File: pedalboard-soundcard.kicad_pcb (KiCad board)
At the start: 2 copper layers, 65 x 56 mm, 81 parts, among them J1 RPi_GPIO, J2 Conn_02x03_Odd_Even, J3 Conn_02x03_Odd_Even, U1 AT24CS01-STUM, U2 NCP163, U3 NCP163, U4 PCM1863DBT, U5 NCP163, U6 PCM5242RHBR, X1 22.5792Mhz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

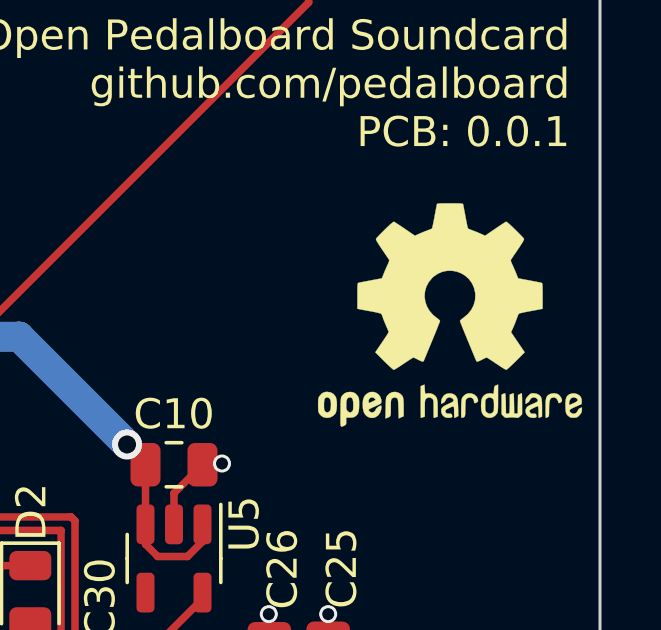
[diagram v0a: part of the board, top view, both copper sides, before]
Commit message: Smaller OSHW Logo
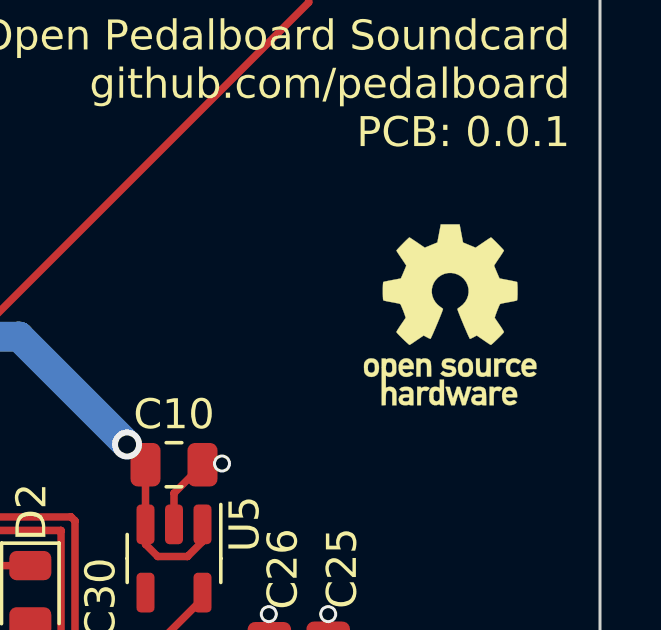
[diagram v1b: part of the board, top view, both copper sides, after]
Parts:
- SYM1: footprint Symbol:OSHW-Logo2_9.8x8mm_SilkScreen -> Symbol:OSHW-Logo_5.7x6mm_SilkScreen

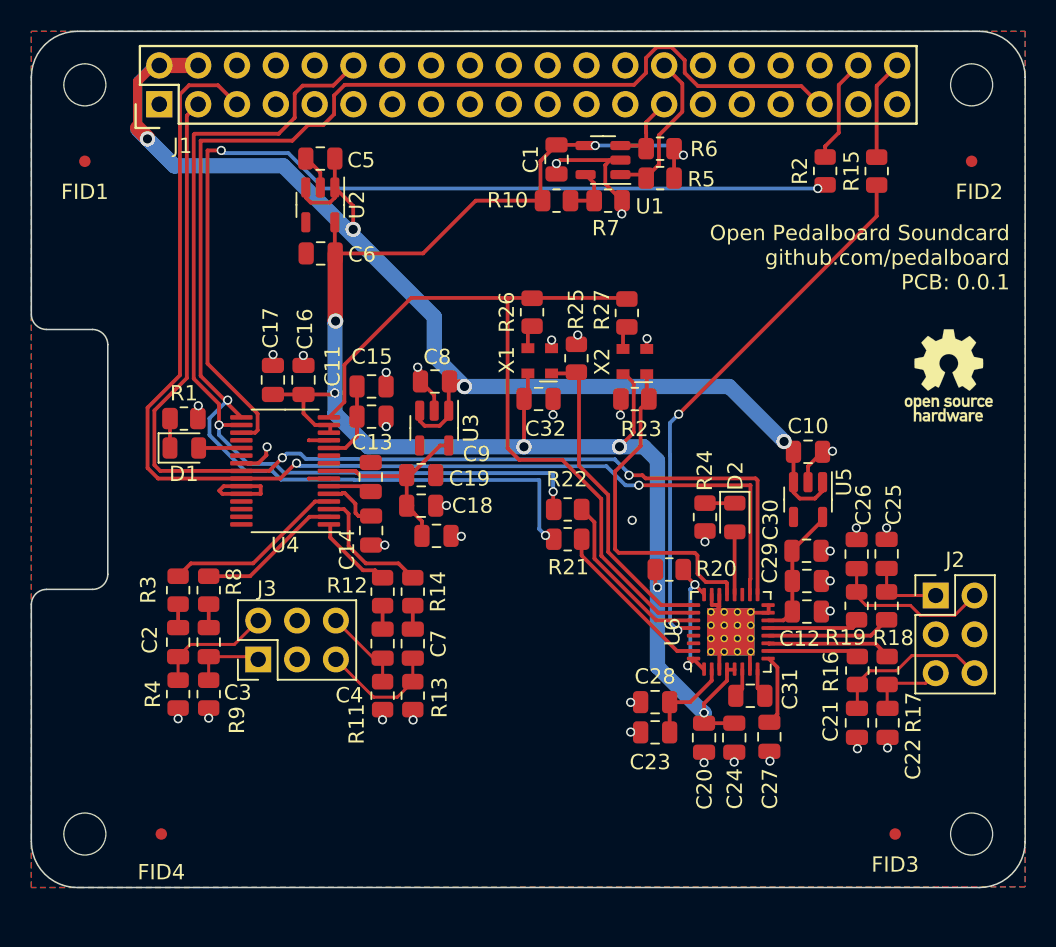
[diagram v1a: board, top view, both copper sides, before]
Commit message: Add texts for connectors
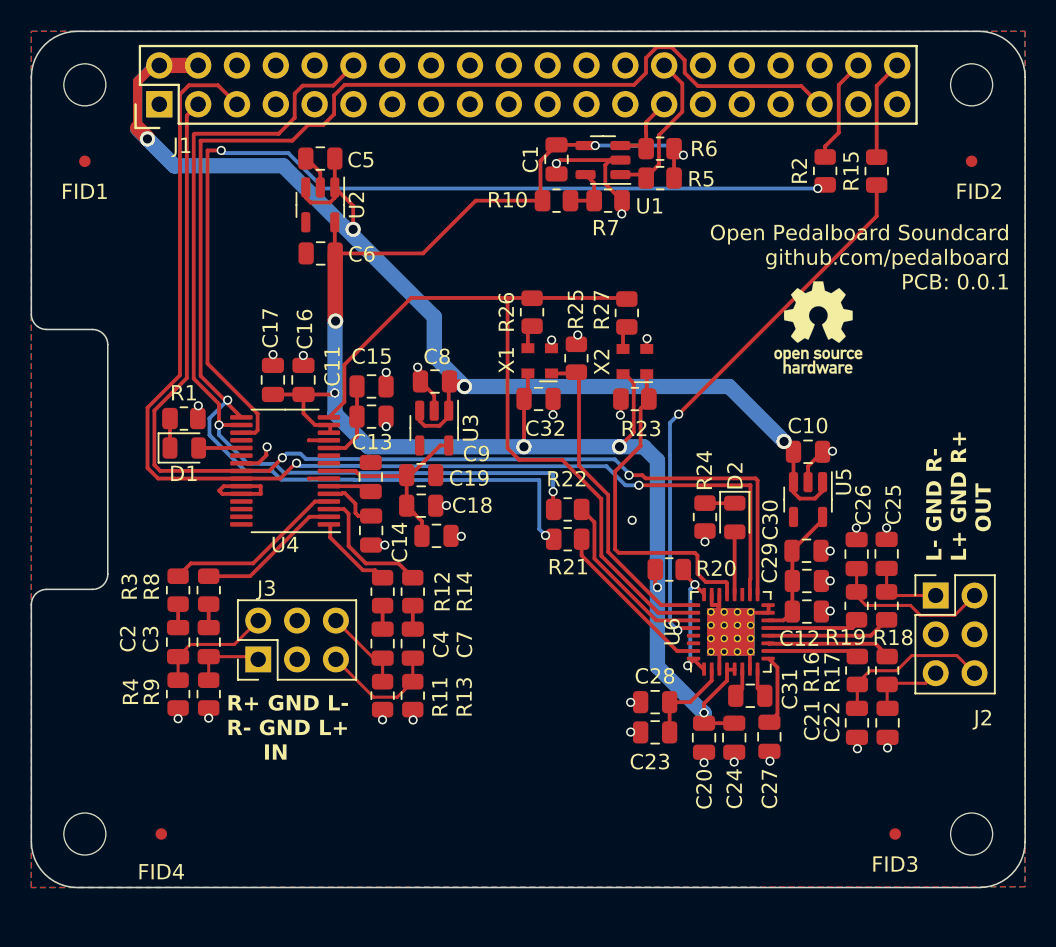
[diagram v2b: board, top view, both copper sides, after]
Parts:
- moved SYM1 9.09 mm to (100.0, 71.9)
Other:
- board text added: "L- GND R- L+ GND R+ OUT"
- board text added: "R+ GND L- R- GND L+ IN"
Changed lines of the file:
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@@
     (property "ki_keywords" "cap capacitor")
     (attr smd)
-    (fp_text reference "C21" (at -0.1 1.72 90) (layer "F.SilkS")
+    (fp_text reference "C21" (at -0.15 2.92 90) (layer "F.SilkS")
         (effects (font (size 1 1) (thickness 0.15)))
     )
@@
     (property "ki_keywords" "R res resistor")
     (attr smd)
-    (fp_text reference "R16" (at 0.075 1.725 90) (layer "F.SilkS")
+    (fp_text reference "R16" (at 0.105 2.975 90) (layer "F.SilkS")
         (effects (font (size 1 1) (thickness 0.15)))
     )
@@
     (property "ki_keywords" "cap capacitor")
     (attr smd)
-    (fp_text reference "C3" (at 3.3 -1.9 -180) (layer "F.SilkS")
+    (fp_text reference "C3" (at -0.2 3.77 -90) (layer "F.SilkS")
         (effects (font (size 1 1) (thickness 0.15)))
     )
@@
     (property "ki_keywords" "cap capacitor")
     (attr smd)
-    (fp_text reference "C14" (at -1.25 -1.575 90) (layer "F.SilkS")
+    (fp_text reference "C14" (at -0.77 1.885 90) (layer "F.SilkS")
         (effects (font (size 1 1) (thickness 0.15)))
     )
@@
     (property "ki_keywords" "cap capacitor")
     (attr smd)
-    (fp_text reference "C4" (at 3.375 2.175 -180) (layer "F.SilkS")
+    (fp_text reference "C4" (at 0.05 -3.845 -90) (layer "F.SilkS")
         (effects (font (size 1 1) (thickness 0.15)))
     )
@@
     (property "ki_keywords" "R res resistor")
     (attr smd)
-    (fp_text reference "R11" (at -1.85 -1.7 90) (layer "F.SilkS")
+    (fp_text reference "R11" (at -0.09 3.775 90) (layer "F.SilkS")
         (effects (font (size 1 1) (thickness 0.15)))
     )
@@
     (property "ki_keywords" "cap capacitor")
     (attr smd)
-    (fp_text reference "C7" (at 0 -1.68 90) (layer "F.SilkS")
+    (fp_text reference "C7" (at 0.05 -3.41 90) (layer "F.SilkS")
         (effects (font (size 1 1) (thickness 0.15)))
     )
@@
     (property "ki_keywords" "R res resistor")
     (attr smd)
-    (fp_text reference "R12" (at -0.4 2.325 -180) (layer "F.SilkS")
+    (fp_text reference "R12" (at 0 -3.925 -90) (layer "F.SilkS")
         (effects (font (size 1 1) (thickness 0.15)))
     )
@@
     (property "ki_keywords" "R res resistor")
     (attr smd)
-    (fp_text reference "R13" (at -0.125 1.75 90) (layer "F.SilkS")
+    (fp_text reference "R13" (at -0.09 3.39 90) (layer "F.SilkS")
         (effects (font (size 1 1) (thickness 0.15)))
     )
@@
   )
   (footprint "Symbol:OSHW-Logo_5.7x6mm_SilkScreen" (layer "F.Cu")
-    (at 108.5 75)
+    (at 99.97 71.87)
     (descr "Open Source Hardware Logo")
     (tags "Logo OSHW")
@@
     (property "ki_keywords" "connector")
     (attr through_hole)
-    (fp_text reference "J2" (at 1.27 -2.33) (layer "F.SilkS")
+    (fp_text reference "J2" (at 3.12 8.03) (layer "F.SilkS")
         (effects (font (size 1 1) (thickness 0.15)))
     )
@@
     (property "ki_keywords" "R res resistor")
     (attr smd)
-    (fp_text reference "R8" (at -0.55 -1.65 90) (layer "F.SilkS")
+    (fp_text reference "R8" (at -0.22 3.72 90) (layer "F.SilkS")
         (effects (font (size 1 1) (thickness 0.15)))
     )
@@
     (property "ki_keywords" "R res resistor")
     (attr smd)
-    (fp_text reference "R14" (at 0 -1.65 90) (layer "F.SilkS")
+    (fp_text reference "R14" (at 0 -3.41 90) (layer "F.SilkS")
         (effects (font (size 1 1) (thickness 0.15)))
     )
@@
     (property "ki_keywords" "cap capacitor")
     (attr smd)
-    (fp_text reference "C22" (at 2.38 -1.67 90) (layer "F.SilkS")
+    (fp_text reference "C22" (at -0.05 3.62 90) (layer "F.SilkS")
         (effects (font (size 1 1) (thickness 0.15)))
     )
@@
     (property "ki_keywords" "R res resistor")
     (attr smd)
-    (fp_text reference "R3" (at -0.025 1.95 90) (layer "F.SilkS")
+    (fp_text reference "R3" (at -0.22 3.16 90) (layer "F.SilkS")
         (effects (font (size 1 1) (thickness 0.15)))
     )
@@
     (property "ki_keywords" "R res resistor")
     (attr smd)
-    (fp_text reference "R17" (at 2.745 -1.725 90) (layer "F.SilkS")
+    (fp_text reference "R17" (at 0.125 3.575 90) (layer "F.SilkS")
         (effects (font (size 1 1) (thickness 0.15)))
     )
@@
     (property "ki_keywords" "R res resistor")
     (attr smd)
-    (fp_text reference "R9" (at -1.7 1.85 90) (layer "F.SilkS")
+    (fp_text reference "R9" (at 0.13 -3.72 90) (layer "F.SilkS")
         (effects (font (size 1 1) (thickness 0.15)))
     )
@@
     (property "ki_keywords" "cap capacitor")
     (attr smd)
-    (fp_text reference "C2" (at -0.15 1.85 90) (layer "F.SilkS")
+    (fp_text reference "C2" (at -0.23 3.26 90) (layer "F.SilkS")
         (effects (font (size 1 1) (thickness 0.15)))
     )
@@
     (property "ki_keywords" "R res resistor")
     (attr smd)
-    (fp_text reference "R4" (at 0 -1.65 90) (layer "F.SilkS")
+    (fp_text reference "R4" (at 0.13 -3.08 90) (layer "F.SilkS")
         (effects (font (size 1 1) (thickness 0.15)))
     )
@@
   (gr_line (start 49.5 89) (end 52.5 89)
     (stroke (width 0.1) (type solid)) (layer "Edge.Cuts"))
+  (gr_text "R+ GND L-\nR- GND L+\n     IN" (at 61.27 100.26) (layer "F.SilkS" knockout)
+    (effects (font (size 1 1) (thickness 0.2) bold) (justify left bottom))
+  )
   (gr_text "${TITLE}\n${COMPANY}\nPCB: ${REVISION}" (at 112.5 69.5) (layer "F.SilkS")
     (effects (font (size 1 1) (thickness 0.15)) (justify right bottom))
   )
+  (gr_text "L- GND R-\nL+ GND R+\n    OUT" (at 111.37 87.18 90) (layer "F.SilkS" knockout)
+    (effects (font (size 1 1) (thickness 0.2) bold) (justify left bottom))
+  )
   (gr_text "Dimensions taken from\nhttps://github.com/raspberrypi/hats/blob/master/hat-board-mechanical.pdf" (at 85 119) (layer "Cmts.User")

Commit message: Revert to standard RPI headers
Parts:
- J2, J3: footprint Connector_PinHeader_2.54mm:PinHeader_2x03_P2.54mm_Vertical -> pedalboard-soundcard:PinSocket_2x03_P2.54mm_Vertical
- moved J2 2.54 mm to (110.2, 89.4)
- moved J3 2.54 mm to (63.3, 91.0)

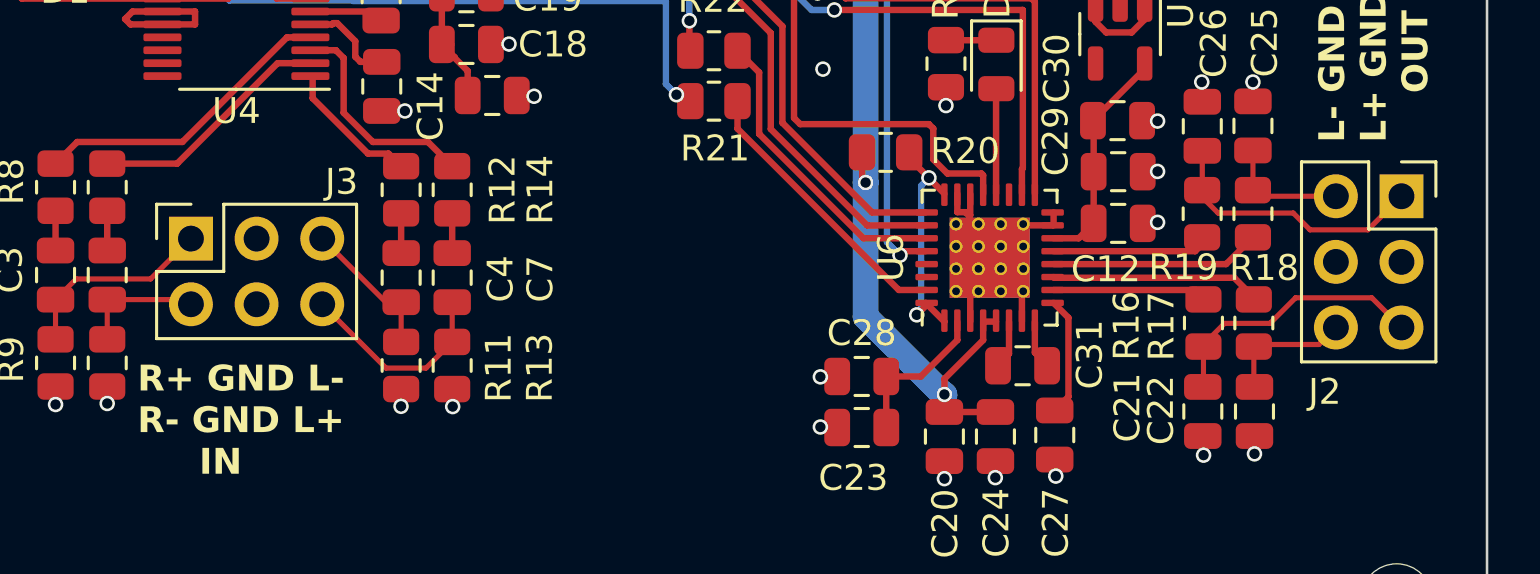
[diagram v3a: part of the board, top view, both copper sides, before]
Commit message: Fix reverted connectors
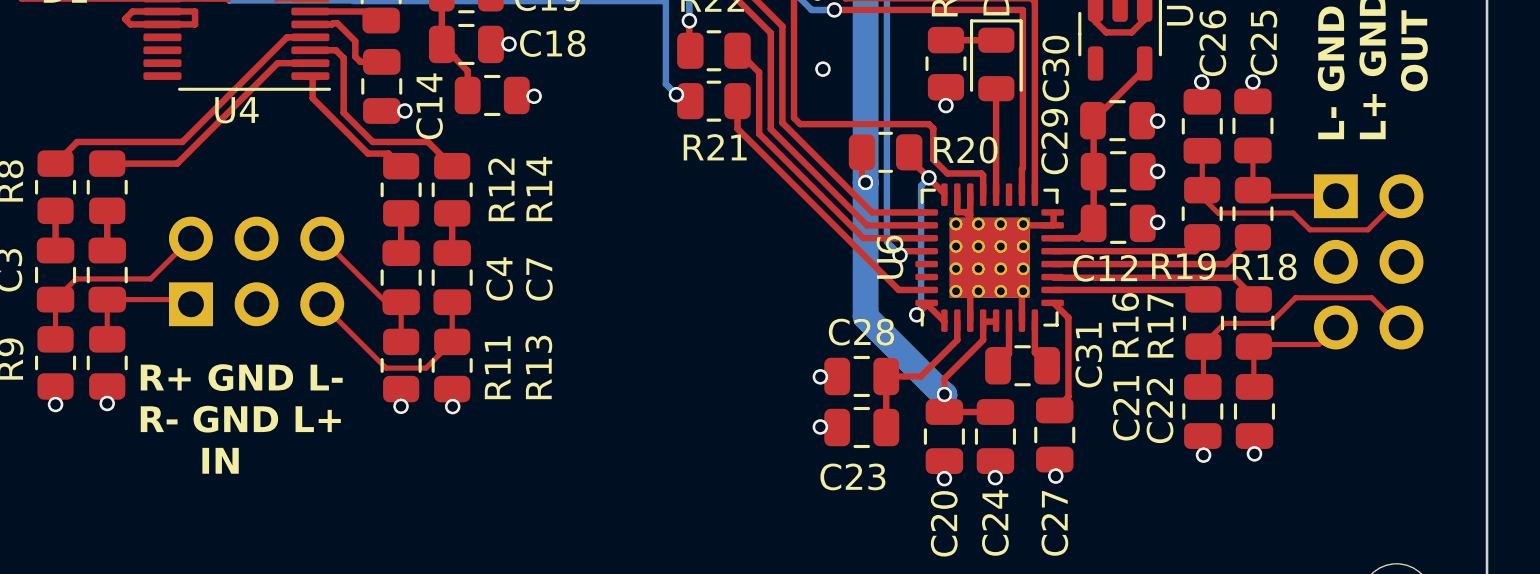
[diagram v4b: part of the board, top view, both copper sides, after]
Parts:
- J2, J3: moved to B.Cu
- moved J2 2.54 mm to (107.7, 89.4), turned to 180 degrees
- moved J3 2.54 mm to (63.3, 93.6), turned to -90 degrees

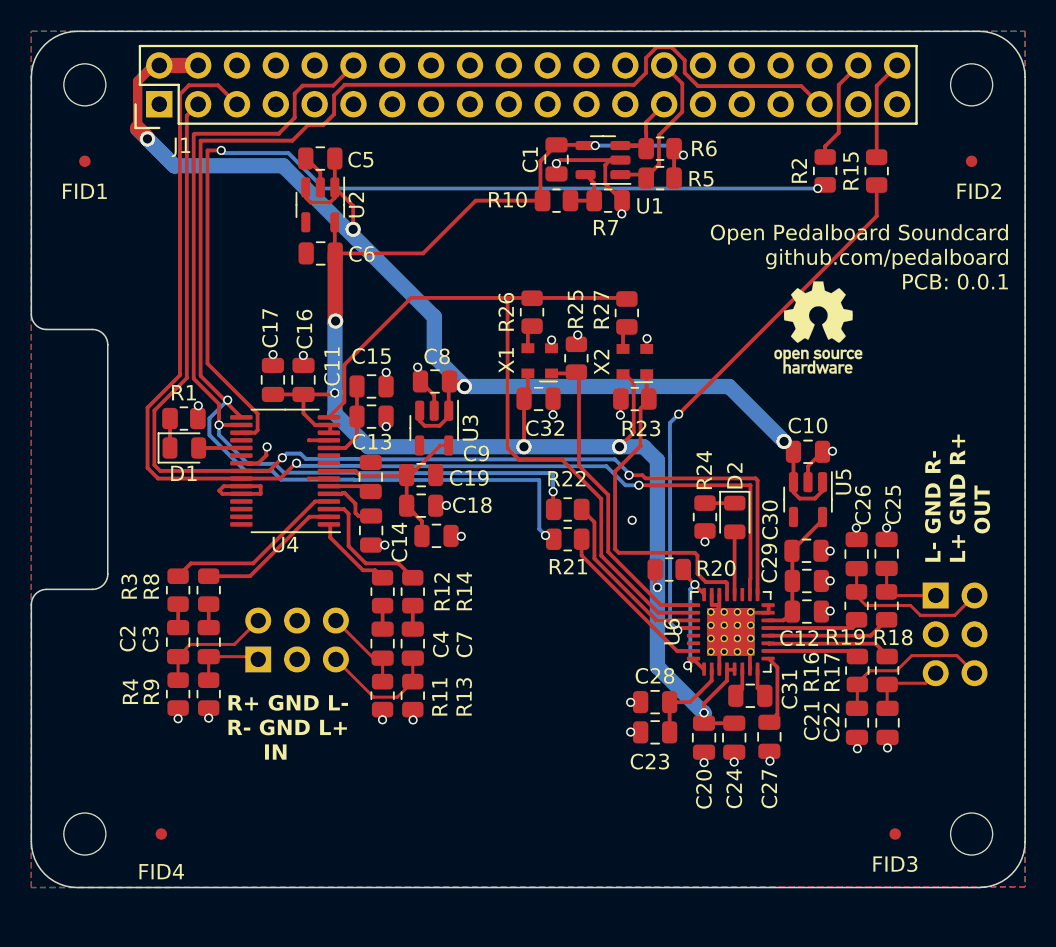
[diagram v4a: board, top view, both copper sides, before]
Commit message: Add 3.5mm jack connectors
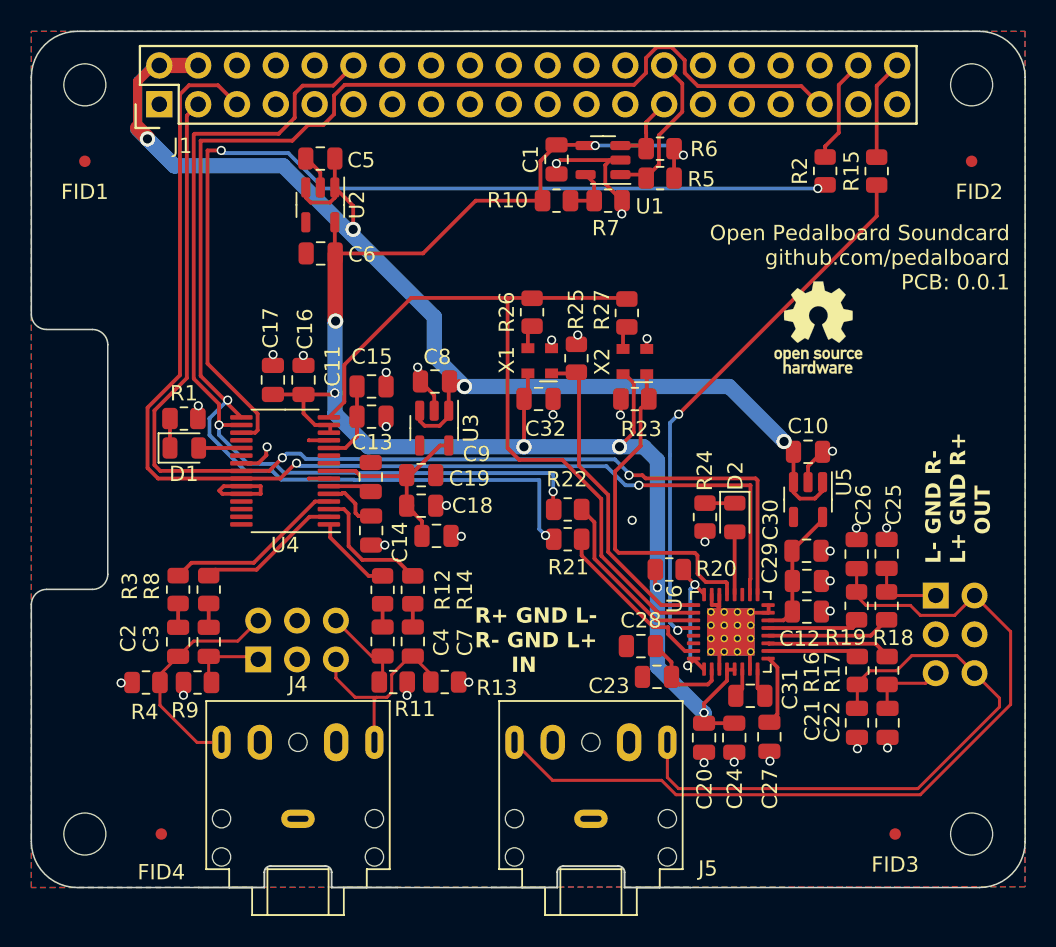
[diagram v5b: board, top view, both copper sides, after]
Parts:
- added J4: Audio_Jack, Connector_Audio:Jack_3.5mm_CUI_SJ1-3525N_Horizontal, F.Cu at (65.9, 104.0)
- added J5: Audio_Jack, Connector_Audio:Jack_3.5mm_CUI_SJ1-3525N_Horizontal, F.Cu at (85.1, 104.0)
- moved C28 3.78 mm to (88.4, 92.7)
- moved C23 3.63 mm to (89.4, 94.7)
- moved R13 2.27 mm to (75.5, 95.1), turned to 180 degrees
- moved R4 2.23 mm to (56.0, 95.1), turned to 0 degrees
- moved R11 1.13 mm to (72.2, 95.1), turned to 180 degrees
- moved R9 1.05 mm to (59.4, 95.1), turned to 0 degrees
- moved C4 0.14 mm to (71.5, 92.4)
- moved C7 0.14 mm to (73.5, 92.4)
- moved R12 0.12 mm to (71.5, 89.0)
- moved R14 0.12 mm to (73.5, 89.0)
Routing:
- net /DAC/outr+: track 10.3 -> 54.7 mm
- net /DAC/outl+: track 10.5 -> 39.9 mm
- net /ADC/inr+: track 7.76 -> 14.9 mm
- net /ADC/inl+: track 8.01 -> 13.8 mm
- net GND: track 62.1 -> 61.1 mm, vias 36 -> 34
- net /ADC/inl-: track 5.61 -> 6.40 mm
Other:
- outline, holes or cut-outs redrawn
